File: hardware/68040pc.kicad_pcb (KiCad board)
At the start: 4 copper layers, 304.8 x 243.8 mm, 17 parts, among them J10 EXP, J11 EXP, J12 EXP, J13 EXP, J14 EXP, J15 EXP, J5 DB25_Receptacle_MountingHoles, J6 DE9_Plug_MountingHoles, J7 DE9_Plug_MountingHoles, J8 EXP, J9 EXP, U1 68LC040, U2 ICE40HX4K-TQ144

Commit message: fix EXP connector positioning
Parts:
- removed the J5 at (337.9, 76.2)
- removed the J6 at (281.9, 76.2)
- removed the J7 at (248.9, 76.2)
- moved J1 74.2 mm to (78.1, 189.0), turned to -90 degrees
- moved J2 74.2 mm to (98.4, 189.0), turned to -90 degrees
- moved J3 74.2 mm to (139.1, 189.0), turned to -90 degrees
- moved J4 74.2 mm to (159.4, 189.0), turned to -90 degrees
- moved J5 74.2 mm to (118.8, 189.0), turned to -90 degrees
- moved J6 74.2 mm to (179.7, 189.0), turned to -90 degrees
- moved J7 74.2 mm to (200.0, 189.0), turned to -90 degrees
- moved J8 6.54 mm to (220.4, 189.0)
- renumbered J8 to J1, J2 to J10, J3 to J11, J4 to J12, J9 to J2, J10 to J3, J11 to J4, J12 to J5, J13 to J6, J14 to J7, J15 to J8, J1 to J9

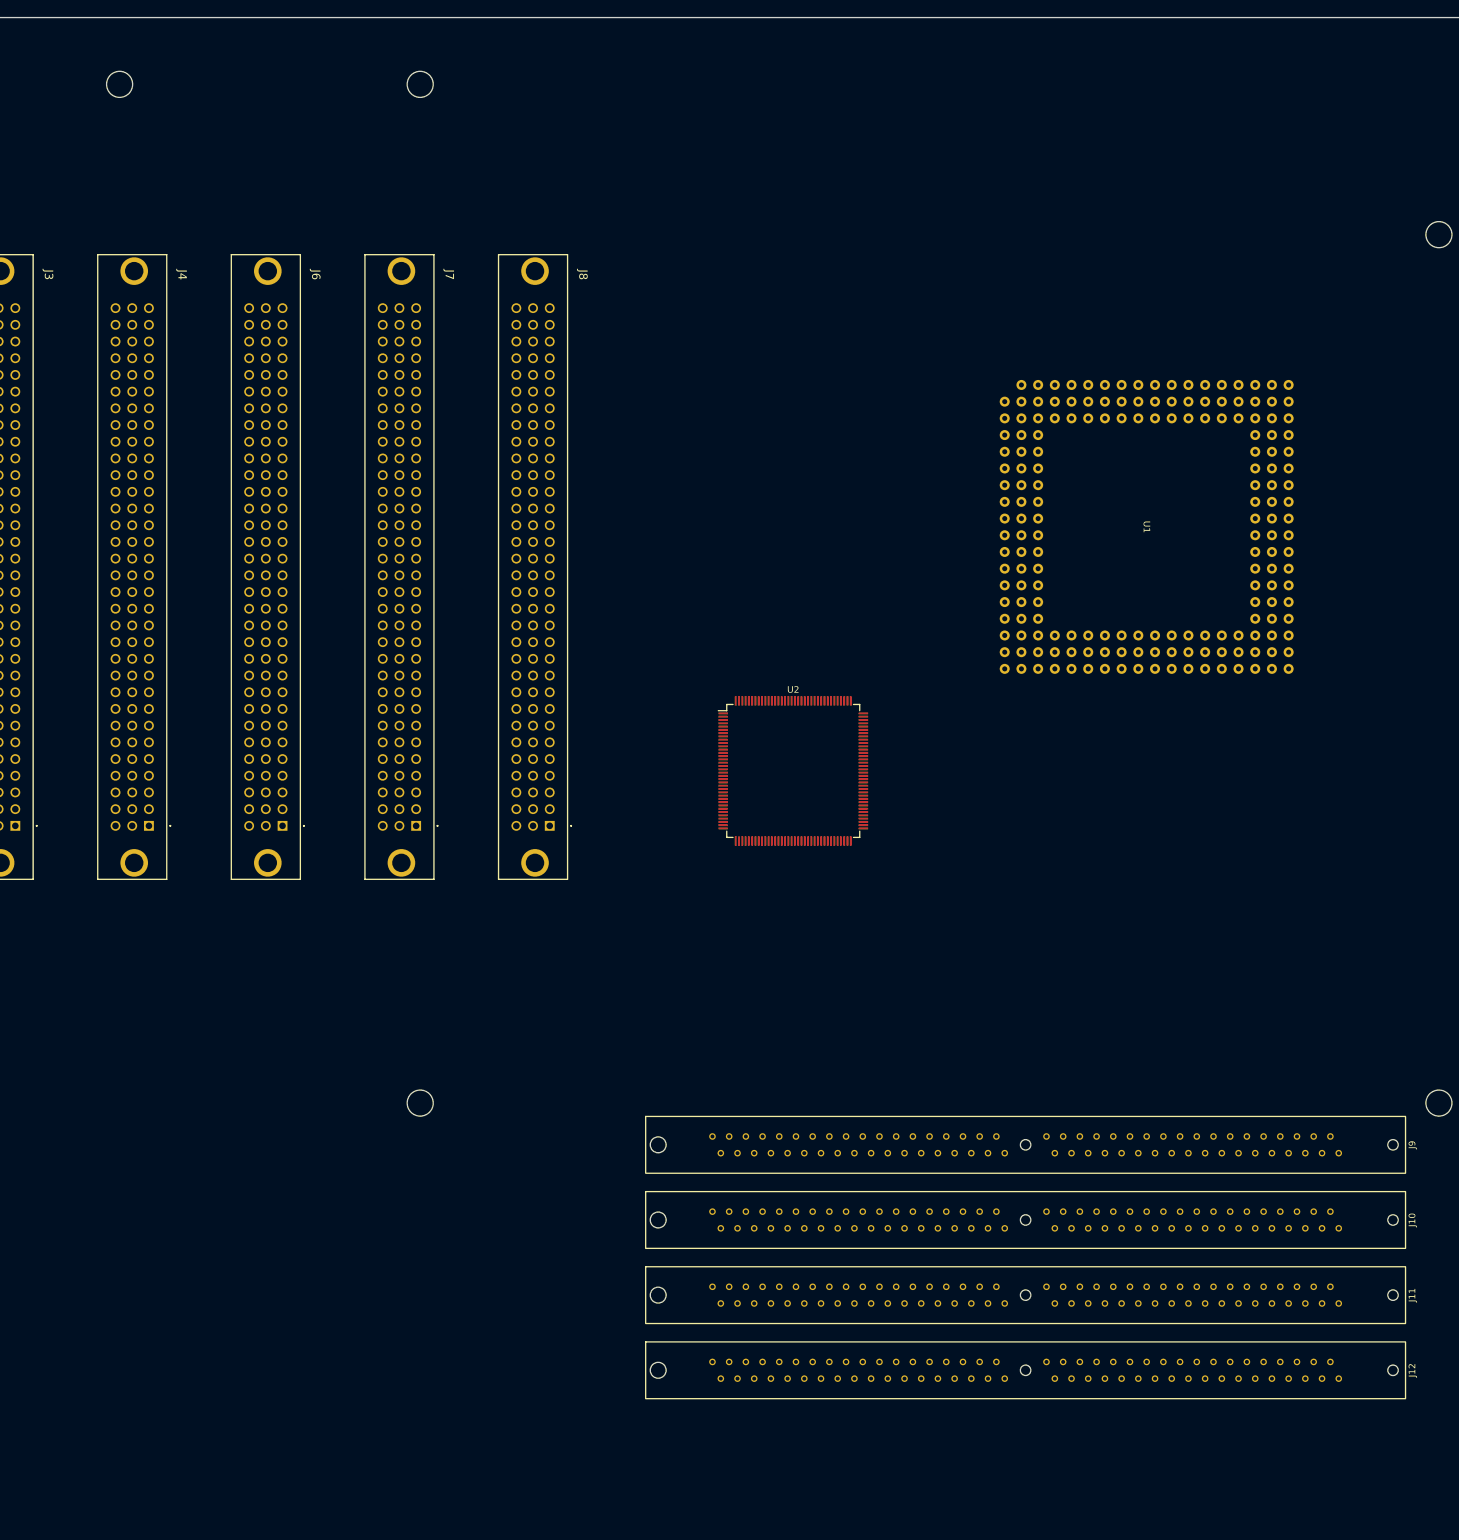
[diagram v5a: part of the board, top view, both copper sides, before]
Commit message: Add 3d models, re-place exp slots, add components
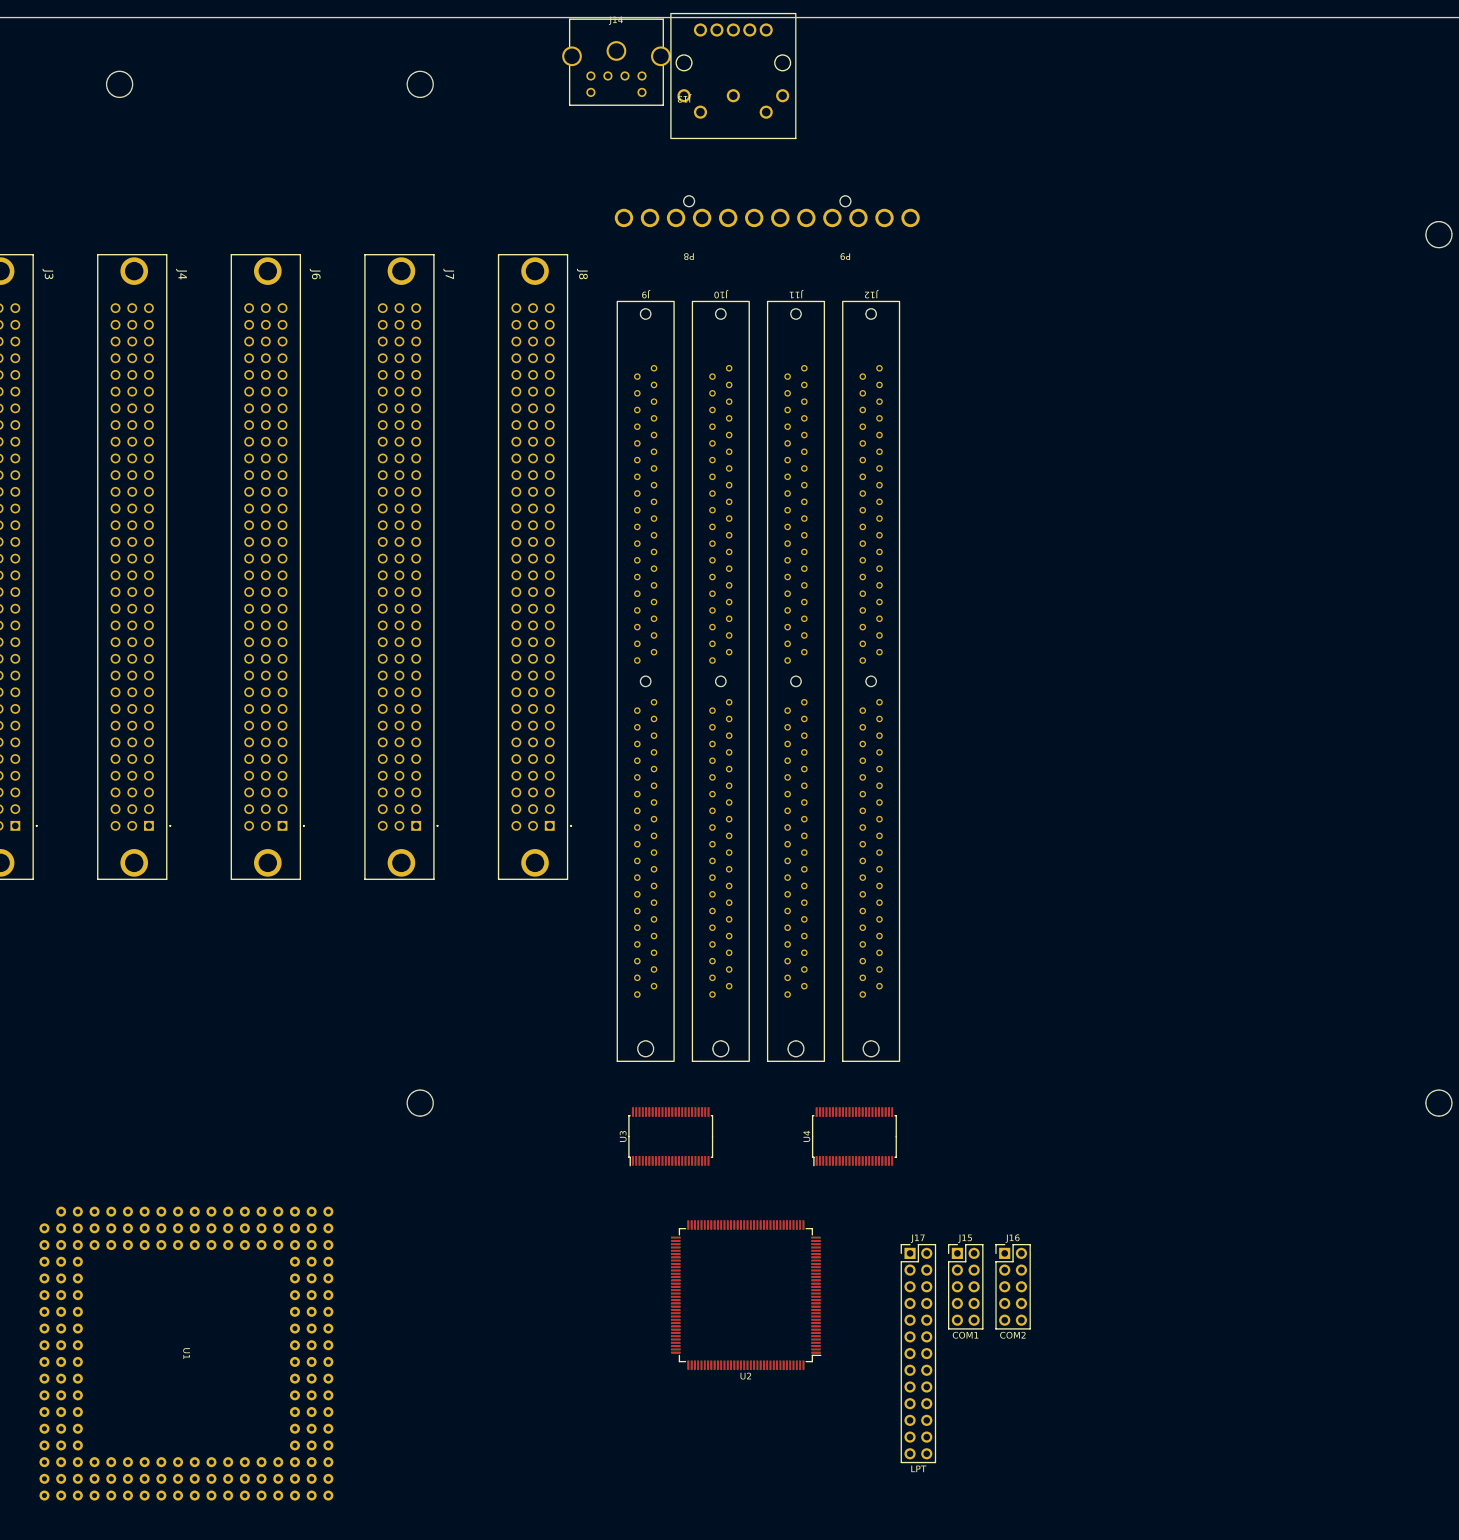
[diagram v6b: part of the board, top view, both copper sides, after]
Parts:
- added J13: DIN-5_180degree, 68040:DIN5-180, F.Cu at (240.8, 77.9)
- added J14: Mini-DIN-6, 68040:Mini-DIN6, F.Cu at (226.6, 74.9)
- added J15: COM1, Connector_PinHeader_2.54mm:PinHeader_2x05_P2.54mm_Vertical, F.Cu at (282.4, 254.0)
- added J16: COM2, Connector_PinHeader_2.54mm:PinHeader_2x05_P2.54mm_Vertical, F.Cu at (289.6, 254.0)
- added J17: LPT, Connector_PinHeader_2.54mm:PinHeader_2x13_P2.54mm_Vertical, F.Cu at (275.2, 254.0)
- added P8: Conn_01x06, 68040:15-48-0106, F.Cu at (231.6, 96.5)
- added P9: Conn_01x06, 68040:15-48-0106, F.Cu at (255.4, 96.5)
- added U3: SN74ALVC164245, Package_SO:TSSOP-48_6.1x12.5mm_P0.5mm, F.Cu at (238.8, 236.2)
- added U4: SN74ALVC164245, Package_SO:TSSOP-48_6.1x12.5mm_P0.5mm, F.Cu at (266.7, 236.2)
- moved U1 192.7 mm to (186.7, 247.7)
- moved J12 168.8 mm to (270.5, 119.4), turned to 90 degrees
- moved J11 163.8 mm to (259.1, 119.4), turned to 90 degrees
- moved J10 160.3 mm to (247.7, 119.4), turned to 90 degrees
- moved J9 158.4 mm to (236.2, 119.4), turned to 90 degrees
- moved U2 80.1 mm to (250.2, 260.4), turned to 180 degrees
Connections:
- J1 pad A10: unconnected-(J1-PadA10) -> /Expansion/D14
- J1 pad A3: unconnected-(J1-PadA3) -> /Expansion/D0
- J1 pad A4: unconnected-(J1-PadA4) -> /Expansion/D2
- J1 pad A5: unconnected-(J1-PadA5) -> /Expansion/D4
- J1 pad A6: unconnected-(J1-PadA6) -> /Expansion/D6
- J1 pad A7: unconnected-(J1-PadA7) -> /Expansion/D8
- J1 pad A8: unconnected-(J1-PadA8) -> /Expansion/D10
- J1 pad A9: unconnected-(J1-PadA9) -> /Expansion/D12
- J1 pad B1: unconnected-(J1-PadB1) -> /Expansion/D16
- J1 pad B10: unconnected-(J1-PadB10) -> /Expansion/D25
- J1 pad B11: unconnected-(J1-PadB11) -> /Expansion/D26
- J1 pad B12: unconnected-(J1-PadB12) -> /Expansion/D27
- J1 pad B13: unconnected-(J1-PadB13) -> /Expansion/D28
- J1 pad B14: unconnected-(J1-PadB14) -> /Expansion/D29
- J1 pad B15: unconnected-(J1-PadB15) -> /Expansion/D30
- J1 pad B16: unconnected-(J1-PadB16) -> /Expansion/D31
- J1 pad B2: unconnected-(J1-PadB2) -> /Expansion/D17
- J1 pad B3: unconnected-(J1-PadB3) -> /Expansion/D18
- J1 pad B4: unconnected-(J1-PadB4) -> /Expansion/D19
- J1 pad B5: unconnected-(J1-PadB5) -> /Expansion/D20
- J1 pad B6: unconnected-(J1-PadB6) -> /Expansion/D21
- J1 pad B7: unconnected-(J1-PadB7) -> /Expansion/D22
- J1 pad B8: unconnected-(J1-PadB8) -> /Expansion/D23
- J1 pad B9: unconnected-(J1-PadB9) -> /Expansion/D24
- J1 pad C10: unconnected-(J1-PadC10) -> /Expansion/D15
- J1 pad C3: unconnected-(J1-PadC3) -> /Expansion/D1
- J1 pad C4: unconnected-(J1-PadC4) -> /Expansion/D3
- J1 pad C5: unconnected-(J1-PadC5) -> /Expansion/D5
- J1 pad C6: unconnected-(J1-PadC6) -> /Expansion/D7
- J1 pad C7: unconnected-(J1-PadC7) -> /Expansion/D9
- J1 pad C8: unconnected-(J1-PadC8) -> /Expansion/D11
- J1 pad C9: unconnected-(J1-PadC9) -> /Expansion/D13
- J1 pad MH1: unconnected-(J1-PadMH1) -> GND
- J1 pad MH2: unconnected-(J1-PadMH2) -> GND
- J10 pad 2: /Memory/D0 -> /Memory/DRAM_D0
- J10 pad 20: /Memory/D4 -> /Memory/DRAM_D4
- J10 pad 21: /Memory/D20 -> /Memory/DRAM_D20
- J10 pad 22: /Memory/D5 -> /Memory/DRAM_D5
- J10 pad 23: /Memory/D21 -> /Memory/DRAM_D21
- J10 pad 24: /Memory/D6 -> /Memory/DRAM_D6
- J10 pad 25: /Memory/D22 -> /Memory/DRAM_D22
- J10 pad 26: /Memory/D7 -> /Memory/DRAM_D7
- J10 pad 27: /Memory/D23 -> /Memory/DRAM_D23
- J10 pad 3: /Memory/D16 -> /Memory/DRAM_D16
- J10 pad 4: /Memory/D1 -> /Memory/DRAM_D1
- J10 pad 49: /Memory/D8 -> /Memory/DRAM_D8
- J10 pad 5: /Memory/D17 -> /Memory/DRAM_D17
- J10 pad 50: /Memory/D24 -> /Memory/DRAM_D24
- J10 pad 51: /Memory/D9 -> /Memory/DRAM_D9
- J10 pad 52: /Memory/D25 -> /Memory/DRAM_D25
- J10 pad 53: /Memory/D10 -> /Memory/DRAM_D10
- J10 pad 54: /Memory/D26 -> /Memory/DRAM_D26
- J10 pad 55: /Memory/D11 -> /Memory/DRAM_D11
- J10 pad 56: /Memory/D27 -> /Memory/DRAM_D27
- J10 pad 57: /Memory/D12 -> /Memory/DRAM_D12
- J10 pad 58: /Memory/D28 -> /Memory/DRAM_D28
- J10 pad 6: /Memory/D2 -> /Memory/DRAM_D2
- J10 pad 60: /Memory/D29 -> /Memory/DRAM_D29
- J10 pad 61: /Memory/D13 -> /Memory/DRAM_D13
- J10 pad 62: /Memory/D30 -> /Memory/DRAM_D30
- J10 pad 63: /Memory/D14 -> /Memory/DRAM_D14
- J10 pad 64: /Memory/D31 -> /Memory/DRAM_D31
- J10 pad 65: /Memory/D15 -> /Memory/DRAM_D15
- J10 pad 7: /Memory/D18 -> /Memory/DRAM_D18
- J10 pad 8: /Memory/D3 -> /Memory/DRAM_D3
- J10 pad 9: /Memory/D19 -> /Memory/DRAM_D19
- J11 pad 2: /Memory/D0 -> /Memory/DRAM_D0
- J11 pad 20: /Memory/D4 -> /Memory/DRAM_D4
- J11 pad 21: /Memory/D20 -> /Memory/DRAM_D20
- J11 pad 22: /Memory/D5 -> /Memory/DRAM_D5
- J11 pad 23: /Memory/D21 -> /Memory/DRAM_D21
- J11 pad 24: /Memory/D6 -> /Memory/DRAM_D6
- J11 pad 25: /Memory/D22 -> /Memory/DRAM_D22
- J11 pad 26: /Memory/D7 -> /Memory/DRAM_D7
- J11 pad 27: /Memory/D23 -> /Memory/DRAM_D23
- J11 pad 3: /Memory/D16 -> /Memory/DRAM_D16
- J11 pad 4: /Memory/D1 -> /Memory/DRAM_D1
- J11 pad 49: /Memory/D8 -> /Memory/DRAM_D8
- J11 pad 5: /Memory/D17 -> /Memory/DRAM_D17
- J11 pad 50: /Memory/D24 -> /Memory/DRAM_D24
- J11 pad 51: /Memory/D9 -> /Memory/DRAM_D9
- J11 pad 52: /Memory/D25 -> /Memory/DRAM_D25
- J11 pad 53: /Memory/D10 -> /Memory/DRAM_D10
- J11 pad 54: /Memory/D26 -> /Memory/DRAM_D26
- J11 pad 55: /Memory/D11 -> /Memory/DRAM_D11
- J11 pad 56: /Memory/D27 -> /Memory/DRAM_D27
- J11 pad 57: /Memory/D12 -> /Memory/DRAM_D12
- J11 pad 58: /Memory/D28 -> /Memory/DRAM_D28
- J11 pad 6: /Memory/D2 -> /Memory/DRAM_D2
- J11 pad 60: /Memory/D29 -> /Memory/DRAM_D29
- J11 pad 61: /Memory/D13 -> /Memory/DRAM_D13
- J11 pad 62: /Memory/D30 -> /Memory/DRAM_D30
- J11 pad 63: /Memory/D14 -> /Memory/DRAM_D14
- J11 pad 64: /Memory/D31 -> /Memory/DRAM_D31
- J11 pad 65: /Memory/D15 -> /Memory/DRAM_D15
- J11 pad 7: /Memory/D18 -> /Memory/DRAM_D18
- J11 pad 8: /Memory/D3 -> /Memory/DRAM_D3
- J11 pad 9: /Memory/D19 -> /Memory/DRAM_D19
- J12 pad 2: /Memory/D0 -> /Memory/DRAM_D0
- J12 pad 20: /Memory/D4 -> /Memory/DRAM_D4
- J12 pad 21: /Memory/D20 -> /Memory/DRAM_D20
- J12 pad 22: /Memory/D5 -> /Memory/DRAM_D5
- J12 pad 23: /Memory/D21 -> /Memory/DRAM_D21
- J12 pad 24: /Memory/D6 -> /Memory/DRAM_D6
- J12 pad 25: /Memory/D22 -> /Memory/DRAM_D22
- J12 pad 26: /Memory/D7 -> /Memory/DRAM_D7
- J12 pad 27: /Memory/D23 -> /Memory/DRAM_D23
- J12 pad 3: /Memory/D16 -> /Memory/DRAM_D16
- J12 pad 4: /Memory/D1 -> /Memory/DRAM_D1
- J12 pad 49: /Memory/D8 -> /Memory/DRAM_D8
- J12 pad 5: /Memory/D17 -> /Memory/DRAM_D17
- J12 pad 50: /Memory/D24 -> /Memory/DRAM_D24
- J12 pad 51: /Memory/D9 -> /Memory/DRAM_D9
- J12 pad 52: /Memory/D25 -> /Memory/DRAM_D25
- J12 pad 53: /Memory/D10 -> /Memory/DRAM_D10
- J12 pad 54: /Memory/D26 -> /Memory/DRAM_D26
- J12 pad 55: /Memory/D11 -> /Memory/DRAM_D11
- J12 pad 56: /Memory/D27 -> /Memory/DRAM_D27
- J12 pad 57: /Memory/D12 -> /Memory/DRAM_D12
- J12 pad 58: /Memory/D28 -> /Memory/DRAM_D28
- J12 pad 6: /Memory/D2 -> /Memory/DRAM_D2
- J12 pad 60: /Memory/D29 -> /Memory/DRAM_D29
- J12 pad 61: /Memory/D13 -> /Memory/DRAM_D13
- J12 pad 62: /Memory/D30 -> /Memory/DRAM_D30
- J12 pad 63: /Memory/D14 -> /Memory/DRAM_D14
- J12 pad 64: /Memory/D31 -> /Memory/DRAM_D31
- J12 pad 65: /Memory/D15 -> /Memory/DRAM_D15
- J12 pad 7: /Memory/D18 -> /Memory/DRAM_D18
- J12 pad 8: /Memory/D3 -> /Memory/DRAM_D3
- J12 pad 9: /Memory/D19 -> /Memory/DRAM_D19
- J2 pad A10: unconnected-(J2-PadA10) -> /Expansion/D14
- J2 pad A3: unconnected-(J2-PadA3) -> /Expansion/D0
- J2 pad A4: unconnected-(J2-PadA4) -> /Expansion/D2
- J2 pad A5: unconnected-(J2-PadA5) -> /Expansion/D4
- J2 pad A6: unconnected-(J2-PadA6) -> /Expansion/D6
- J2 pad A7: unconnected-(J2-PadA7) -> /Expansion/D8
- J2 pad A8: unconnected-(J2-PadA8) -> /Expansion/D10
- J2 pad A9: unconnected-(J2-PadA9) -> /Expansion/D12
- J2 pad B1: unconnected-(J2-PadB1) -> /Expansion/D16
- J2 pad B10: unconnected-(J2-PadB10) -> /Expansion/D25
- J2 pad B11: unconnected-(J2-PadB11) -> /Expansion/D26
- J2 pad B12: unconnected-(J2-PadB12) -> /Expansion/D27
- J2 pad B13: unconnected-(J2-PadB13) -> /Expansion/D28
- J2 pad B14: unconnected-(J2-PadB14) -> /Expansion/D29
- J2 pad B15: unconnected-(J2-PadB15) -> /Expansion/D30
- J2 pad B16: unconnected-(J2-PadB16) -> /Expansion/D31
- J2 pad B2: unconnected-(J2-PadB2) -> /Expansion/D17
- J2 pad B3: unconnected-(J2-PadB3) -> /Expansion/D18
- J2 pad B4: unconnected-(J2-PadB4) -> /Expansion/D19
- J2 pad B5: unconnected-(J2-PadB5) -> /Expansion/D20
- J2 pad B6: unconnected-(J2-PadB6) -> /Expansion/D21
- J2 pad B7: unconnected-(J2-PadB7) -> /Expansion/D22
- J2 pad B8: unconnected-(J2-PadB8) -> /Expansion/D23
- J2 pad B9: unconnected-(J2-PadB9) -> /Expansion/D24
- J2 pad C10: unconnected-(J2-PadC10) -> /Expansion/D15
- J2 pad C3: unconnected-(J2-PadC3) -> /Expansion/D1
- J2 pad C4: unconnected-(J2-PadC4) -> /Expansion/D3
- J2 pad C5: unconnected-(J2-PadC5) -> /Expansion/D5
- J2 pad C6: unconnected-(J2-PadC6) -> /Expansion/D7
- J2 pad C7: unconnected-(J2-PadC7) -> /Expansion/D9
- J2 pad C8: unconnected-(J2-PadC8) -> /Expansion/D11
- J2 pad C9: unconnected-(J2-PadC9) -> /Expansion/D13
- J2 pad MH1: unconnected-(J2-PadMH1) -> GND
- J2 pad MH2: unconnected-(J2-PadMH2) -> GND
- J9 pad 2: /Memory/D0 -> /Memory/DRAM_D0
- J9 pad 20: /Memory/D4 -> /Memory/DRAM_D4
- J9 pad 21: /Memory/D20 -> /Memory/DRAM_D20
- J9 pad 22: /Memory/D5 -> /Memory/DRAM_D5
- J9 pad 23: /Memory/D21 -> /Memory/DRAM_D21
- J9 pad 24: /Memory/D6 -> /Memory/DRAM_D6
- J9 pad 25: /Memory/D22 -> /Memory/DRAM_D22
- J9 pad 26: /Memory/D7 -> /Memory/DRAM_D7
- J9 pad 27: /Memory/D23 -> /Memory/DRAM_D23
- J9 pad 3: /Memory/D16 -> /Memory/DRAM_D16
- J9 pad 4: /Memory/D1 -> /Memory/DRAM_D1
- J9 pad 49: /Memory/D8 -> /Memory/DRAM_D8
- J9 pad 5: /Memory/D17 -> /Memory/DRAM_D17
- J9 pad 50: /Memory/D24 -> /Memory/DRAM_D24
- J9 pad 51: /Memory/D9 -> /Memory/DRAM_D9
- J9 pad 52: /Memory/D25 -> /Memory/DRAM_D25
- J9 pad 53: /Memory/D10 -> /Memory/DRAM_D10
- J9 pad 54: /Memory/D26 -> /Memory/DRAM_D26
- J9 pad 55: /Memory/D11 -> /Memory/DRAM_D11
- J9 pad 56: /Memory/D27 -> /Memory/DRAM_D27
- J9 pad 57: /Memory/D12 -> /Memory/DRAM_D12
- J9 pad 58: /Memory/D28 -> /Memory/DRAM_D28
- J9 pad 6: /Memory/D2 -> /Memory/DRAM_D2
- J9 pad 60: /Memory/D29 -> /Memory/DRAM_D29
- J9 pad 61: /Memory/D13 -> /Memory/DRAM_D13
- J9 pad 62: /Memory/D30 -> /Memory/DRAM_D30
- J9 pad 63: /Memory/D14 -> /Memory/DRAM_D14
- J9 pad 64: /Memory/D31 -> /Memory/DRAM_D31
- J9 pad 65: /Memory/D15 -> /Memory/DRAM_D15
- J9 pad 7: /Memory/D18 -> /Memory/DRAM_D18
- J9 pad 8: /Memory/D3 -> /Memory/DRAM_D3
- J9 pad 9: /Memory/D19 -> /Memory/DRAM_D19

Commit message: resize board to Baby-AT
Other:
- board size 304.8 x 243.8 mm -> 221 x 243.8 mm
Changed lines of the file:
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@@
     )
   )
-  (gr_rect (start 208.1784 44.196) (end 366.9284 63.4492)
-    (stroke (width 0.15) (type default)) (fill none) (layer "Cmts.User"))
   (gr_rect locked (start 201.35088 45.72) (end 202.95088 238.76)
     (stroke (width 0.15) (type default)) (fill none) (layer "Cmts.User"))
@@
   (gr_circle locked (center 200.66 76.2) (end 202.6412 76.2)
     (stroke (width 0.1) (type default)) (fill none) (layer "Edge.Cuts"))
-  (gr_circle locked (center 355.6 303.53) (end 357.5812 303.53)
-    (stroke (width 0.1) (type default)) (fill none) (layer "Edge.Cuts"))
-  (gr_line locked (start 63.5 309.88) (end 360.68 309.88)
+  (gr_line locked (start 63.5 309.88) (end 276.86 309.88)
     (stroke (width 0.1) (type default)) (layer "Edge.Cuts"))
   (gr_circle locked (center 76.2 231.14) (end 78.1812 231.14)
     (stroke (width 0.1) (type default)) (fill none) (layer "Edge.Cuts"))
-  (gr_arc locked (start 364.49 306.07) (mid 363.374077 308.764077) (end 360.68 309.88)
+  (gr_arc locked (start 280.67 306.07) (mid 279.554077 308.764077) (end 276.86 309.88)
     (stroke (width 0.1) (type default)) (layer "Edge.Cuts"))
   (gr_circle locked (center 76.2 76.2) (end 78.1812 76.2)
@@
   (gr_arc locked (start 59.69 69.85) (mid 60.805923 67.155923) (end 63.5 66.04)
     (stroke (width 0.1) (type default)) (layer "Edge.Cuts"))
-  (gr_line locked (start 364.49 306.07) (end 364.49 69.85)
-    (stroke (width 0.1) (type default)) (layer "Edge.Cuts"))
   (gr_arc locked (start 63.5 309.88) (mid 60.805923 308.764077) (end 59.69 306.07)
     (stroke (width 0.1) (type default)) (layer "Edge.Cuts"))
-  (gr_arc locked (start 360.68 66.04) (mid 363.374077 67.155923) (end 364.49 69.85)
+  (gr_line locked (start 280.67 69.85) (end 280.67 306.07)
     (stroke (width 0.1) (type default)) (layer "Edge.Cuts"))
-  (gr_circle locked (center 355.6 231.14) (end 357.5812 231.14)
-    (stroke (width 0.1) (type default)) (fill none) (layer "Edge.Cuts"))
-  (gr_line locked (start 360.68 66.04) (end 63.5 66.04)
+  (gr_arc locked (start 276.86 66.04) (mid 279.554077 67.155923) (end 280.67 69.85)
+    (stroke (width 0.1) (type default)) (layer "Edge.Cuts"))
+  (gr_line locked (start 276.86 66.04) (end 63.5 66.04)
     (stroke (width 0.1) (type default)) (layer "Edge.Cuts"))
   (gr_circle locked (center 76.2 303.53) (end 78.1812 303.53)
     (stroke (width 0.1) (type default)) (fill none) (layer "Edge.Cuts"))
-  (gr_circle locked (center 355.6 99.06) (end 357.5812 99.06)
-    (stroke (width 0.1) (type default)) (fill none) (layer "Edge.Cuts"))
   (gr_circle locked (center 154.94 76.2) (end 156.9212 76.2)
